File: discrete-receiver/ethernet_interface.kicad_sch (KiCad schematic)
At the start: 16 parts, among them J4 RJ45_Hanrun_HR911105A_Horizon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, J6 SI-52003-F, U11 Ag9905LP, U9 LAN8720A

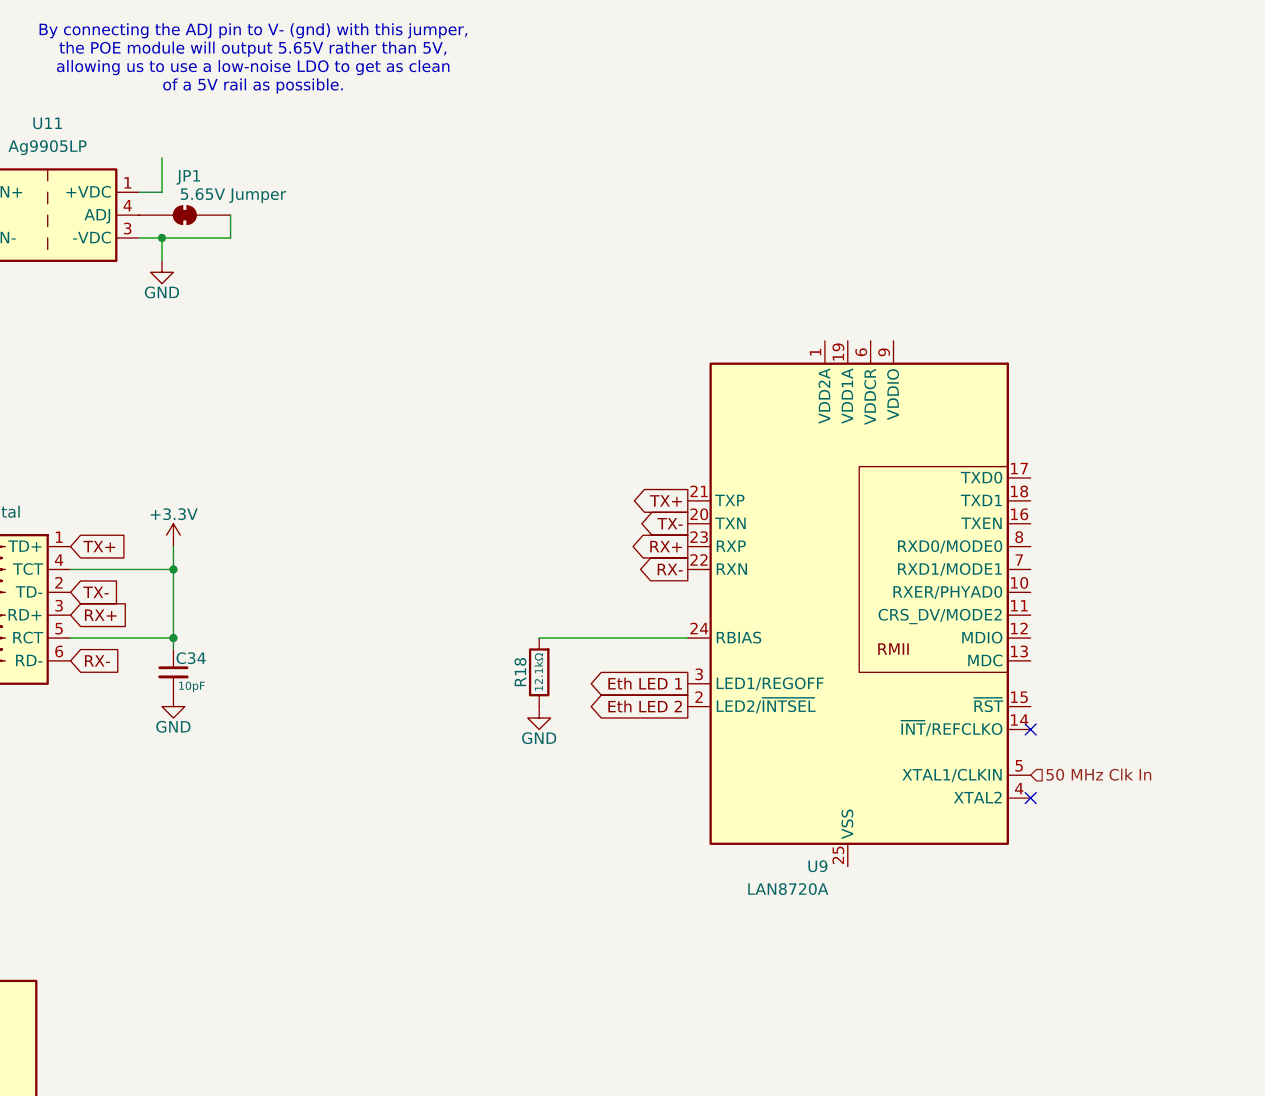
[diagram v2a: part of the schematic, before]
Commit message: Finished Ethernet Hardware Implementation
Ethernet is now implemented using the LAN8720a IC as well as the RP2350's PIO blocks to hopefully support full speed transfer of 192kHz 24 bit stereo audio, as well as control and maybe even a web interface.
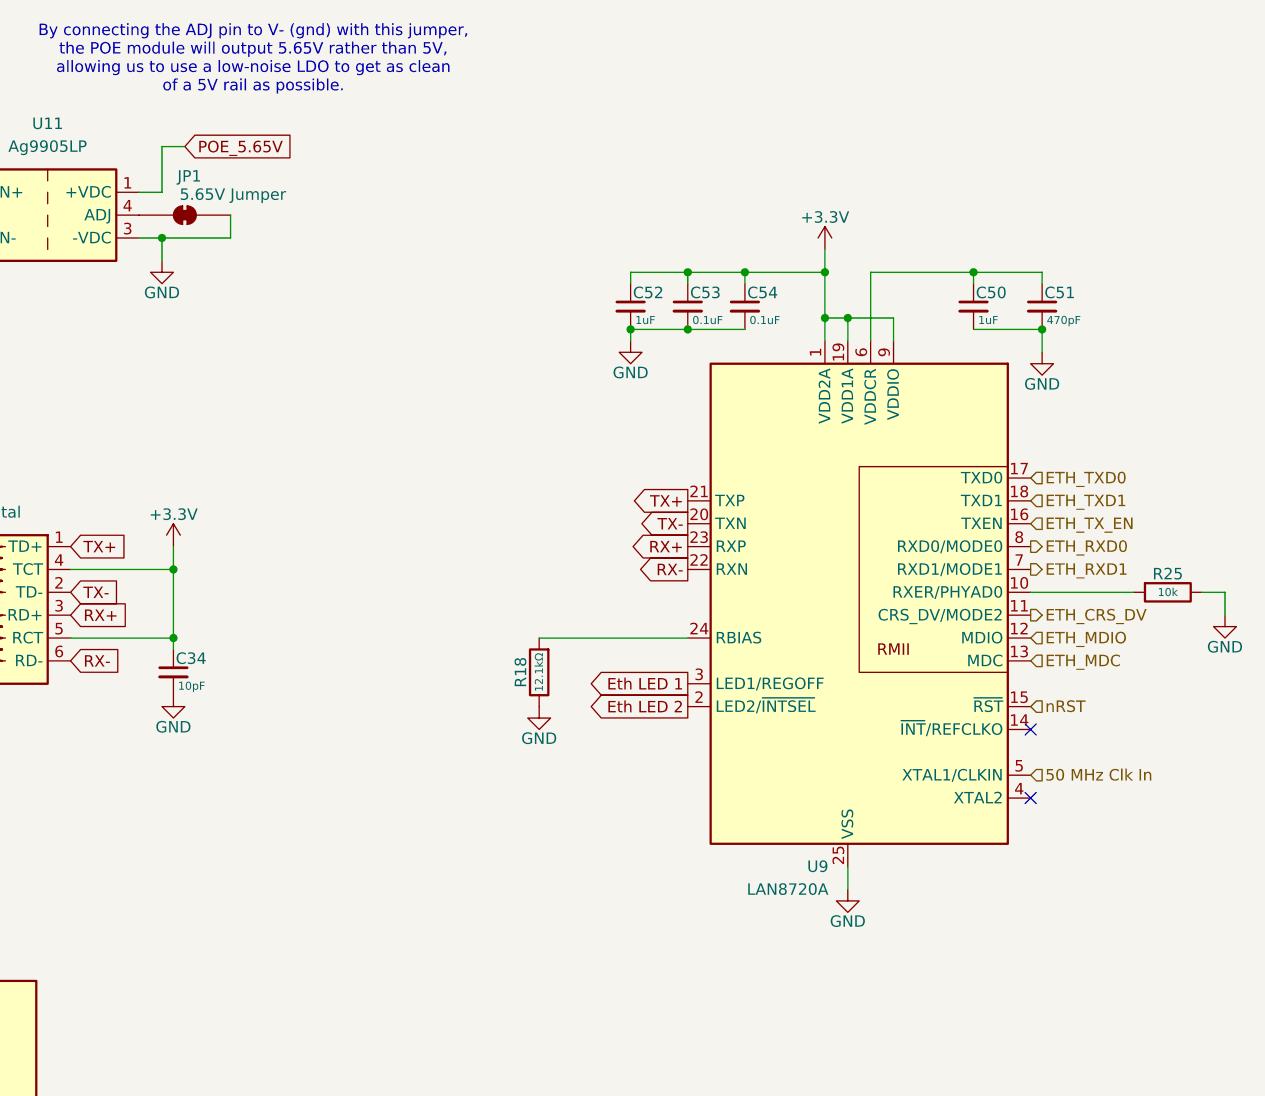
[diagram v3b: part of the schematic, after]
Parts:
- added C50, C52: 1uF, symbol Device:C_Small
- added C51: 470pF, symbol Device:C_Small
- added C53, C54: 0.1uF, symbol Device:C_Small
- added R25: 10k, symbol Device:R
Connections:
- net +3.3V: now also U9.1 (VDD2A), U9.19 (VDD1A), U9.9 (VDDIO), C52.1, C53.1, C54.1
- net GND: now also U9.25 (VSS), C50.2, C51.2, C52.2, C53.2, C54.2, R25.1
- net at U9.10 (RXER/PHYAD0): now also R25.2
- net ETH_CRS_DV: now reaches U9.11 (CRS_DV/MODE2)
- net ETH_MDIO: now reaches U9.12 (MDIO)
- net ETH_MDC: now reaches U9.13 (MDC)
- net nRST: now reaches U9.15 (~{RST})
- net ETH_TX_EN: now reaches U9.16 (TXEN)
- net ETH_TXD0: now reaches U9.17 (TXD0)
- net ETH_TXD1: now reaches U9.18 (TXD1)
- net at U9.6 (VDDCR): now also C50.1, C51.1
- net ETH_RXD1: now reaches U9.7 (RXD1/MODE1)
- net ETH_RXD0: now reaches U9.8 (RXD0/MODE0)
- net POE_5.65V: now reaches U11.1 (+VDC), U11.2 (+VDC)

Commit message: Fixed a couple bugs
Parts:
- removed C34: 10pF, symbol Device:C_Small
- removed J4: RJ45_Hanrun_HR911105A_Horizontal, Connector_RJ:RJ45_Hanrun_HR911105A_Horizontal, symbol Connector:RJ45_Hanrun_HR911105A_Horizontal
- removed R16, R17: 100Ω, symbol Device:R
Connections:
- net 50 MHz Clk In renamed 50 MHz Clk
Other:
- note removed: "unsure if LEDs are connected to correct pins"

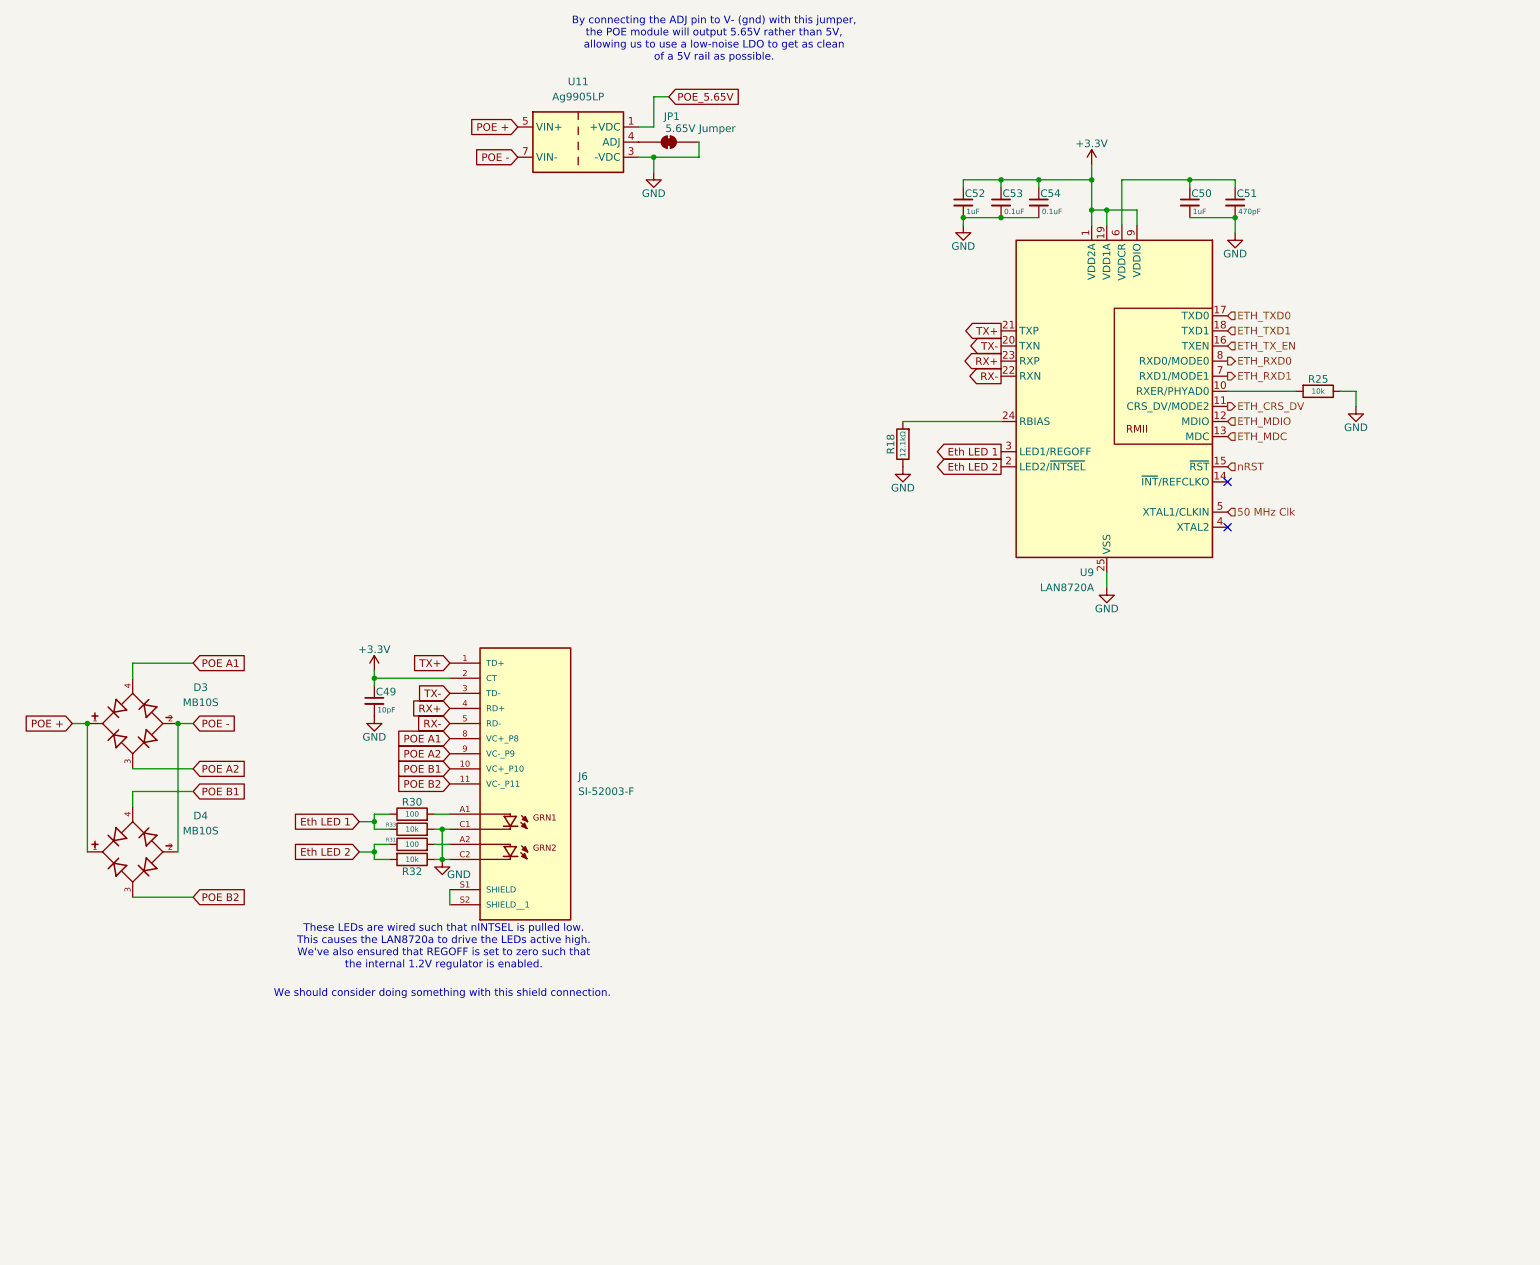
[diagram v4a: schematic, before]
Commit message: Organized Schematic
Standardized component labelling and font sizes. Added descriptions to some sub sheets and organized layout of root sheet.
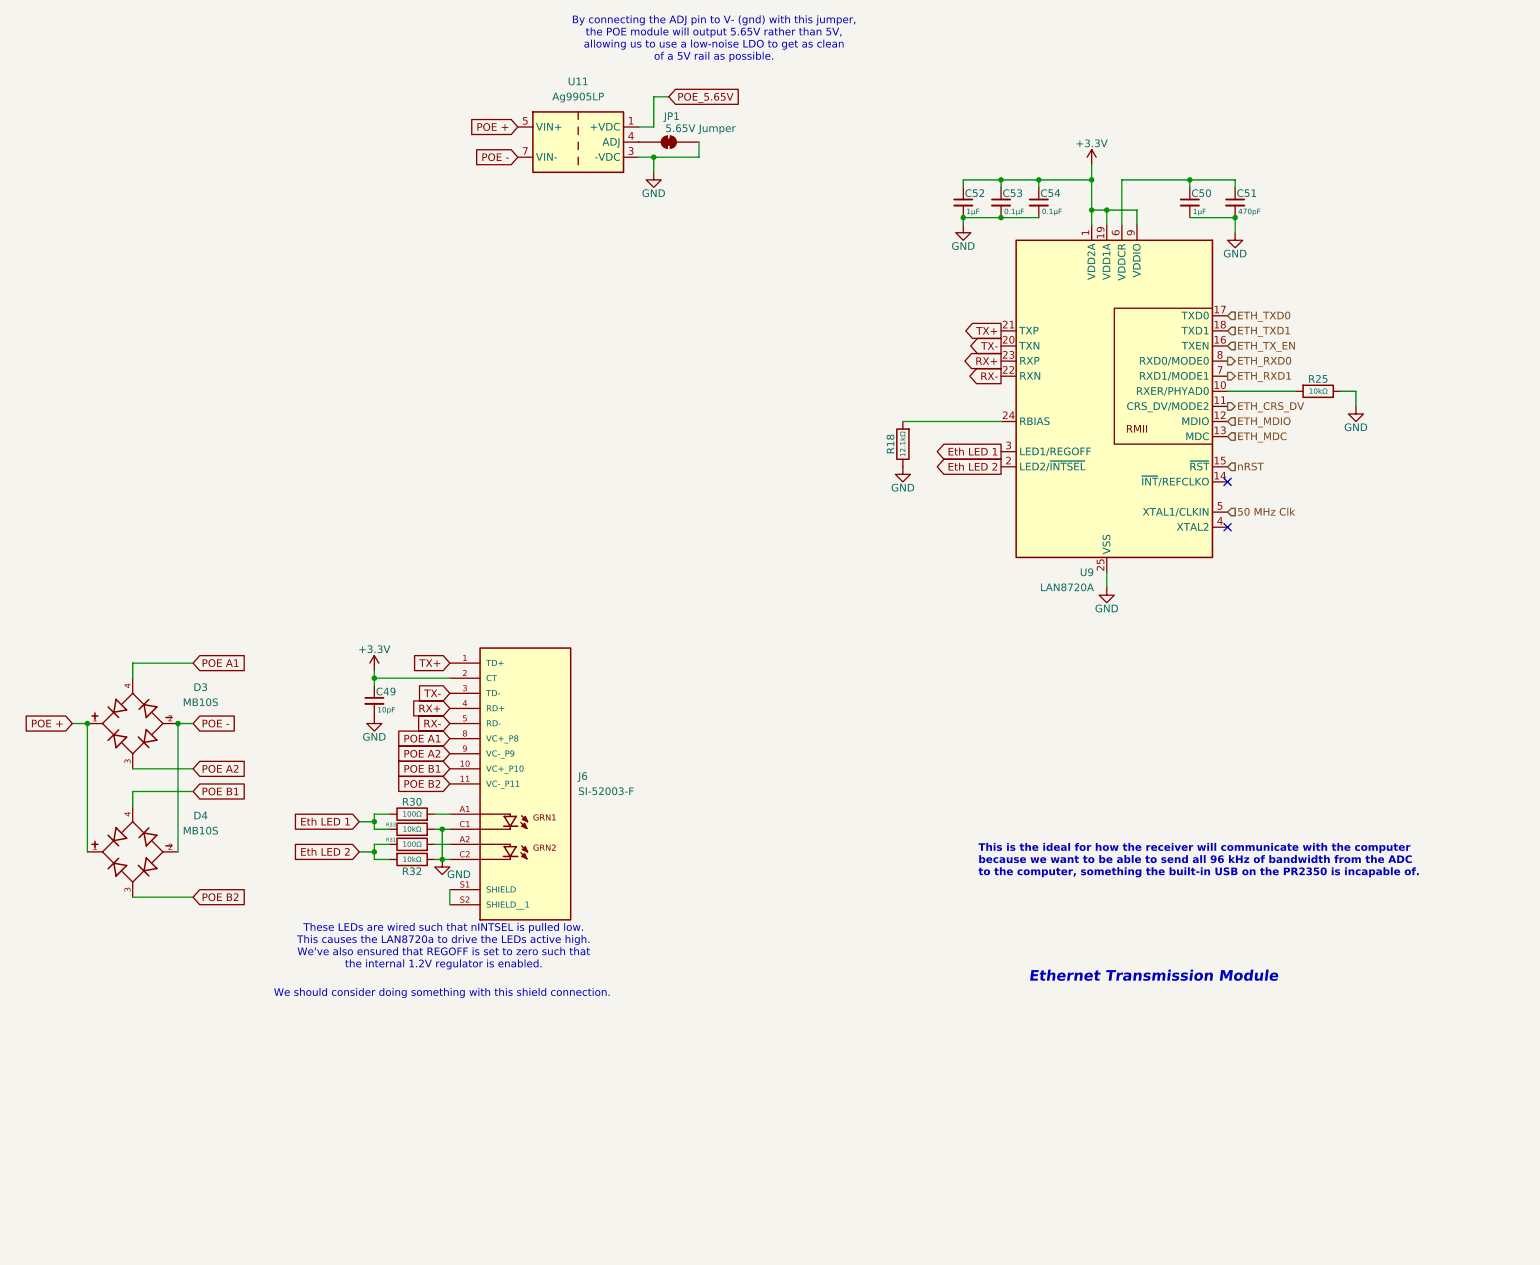
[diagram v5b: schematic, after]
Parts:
- C50, C52: value 1uF -> 1µF
- C53, C54: value 0.1uF -> 0.1µF
- R25, R32, R33: value 10k -> 10kΩ
- R30, R31: value 100 -> 100Ω
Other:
- note added: "Ethernet Transmission Module"
- note added: "This is the ideal for how the receiver will communicate with the computer because we want to be able to send all 96 kHz of bandwidth from the ADC to the computer, something the built-in USB on the PR2350 is incapable of."
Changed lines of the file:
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@@
 		)
 	)
+	(text "Ethernet Transmission Module "
+		(exclude_from_sim no)
+		(at 207.264 189.992 0)
+		(effects
+			(font
+				(size 1.778 1.778)
+				(thickness 0.3556)
+				(bold yes)
+				(italic yes)
+			)
+		)
+	)
+	(text "This is the ideal for how the receiver will communicate with the computer \nbecause we want to be able to send all 96 kHz of bandwidth from the ADC \nto the computer, something the built-in USB on the PR2350 is incapable of."
+		(exclude_from_sim no)
+		(at 177.8 170.434 0)
+		(effects
+			(font
+				(size 1.27 1.27)
+				(thickness 0.254)
+				(bold yes)
+			)
+			(justify left)
+		)
+	)
 	(text "We should consider doing something with this shield connection."
 		(exclude_from_sim no)
@@
 			)
 		)
-		(property "Value" "0.1uF"
+		(property "Value" "0.1µF"
 			(at 188.468 61.214 0)
 			(show_name no)
@@
 			)
 		)
-		(property "Value" "0.1uF"
+		(property "Value" "0.1µF"
 			(at 182.118 61.214 0)
 			(show_name no)
@@
 			)
 		)
-		(property "Value" "10k"
+		(property "Value" "10kΩ"
 			(at 234.95 91.44 90)
 			(show_name no)
@@
 			)
 		)
-		(property "Value" "1uF"
+		(property "Value" "1µF"
 			(at 175.768 61.214 0)
 			(show_name no)
@@
 			)
 		)
-		(property "Value" "100"
+		(property "Value" "100Ω"
 			(at 82.55 167.64 90)
 			(show_name no)
@@
 			)
 		)
-		(property "Value" "10k"
+		(property "Value" "10kΩ"
 			(at 82.55 165.1 90)
 			(show_name no)
@@
 			)
 		)
-		(property "Value" "10k"
+		(property "Value" "10kΩ"
 			(at 82.55 170.18 90)
 			(show_name no)
@@
 			)
 		)
-		(property "Value" "1uF"
+		(property "Value" "1µF"
 			(at 213.868 61.214 0)
 			(show_name no)
@@
 			)
 		)
-		(property "Value" "100"
+		(property "Value" "100Ω"
 			(at 82.55 162.56 90)
 			(show_name no)
